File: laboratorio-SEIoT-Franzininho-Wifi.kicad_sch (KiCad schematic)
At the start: 139 parts, among them J1 Conn_01x20, J2 Conn_01x20, J3 Grove, J4 Grove, M1 Motor_Servo, Q1 BC547, SW1 SW_Push_Dual, SW10 SW_Push_Dual, SW11 SW_Push_Dual, SW12 SW_Push_Dual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

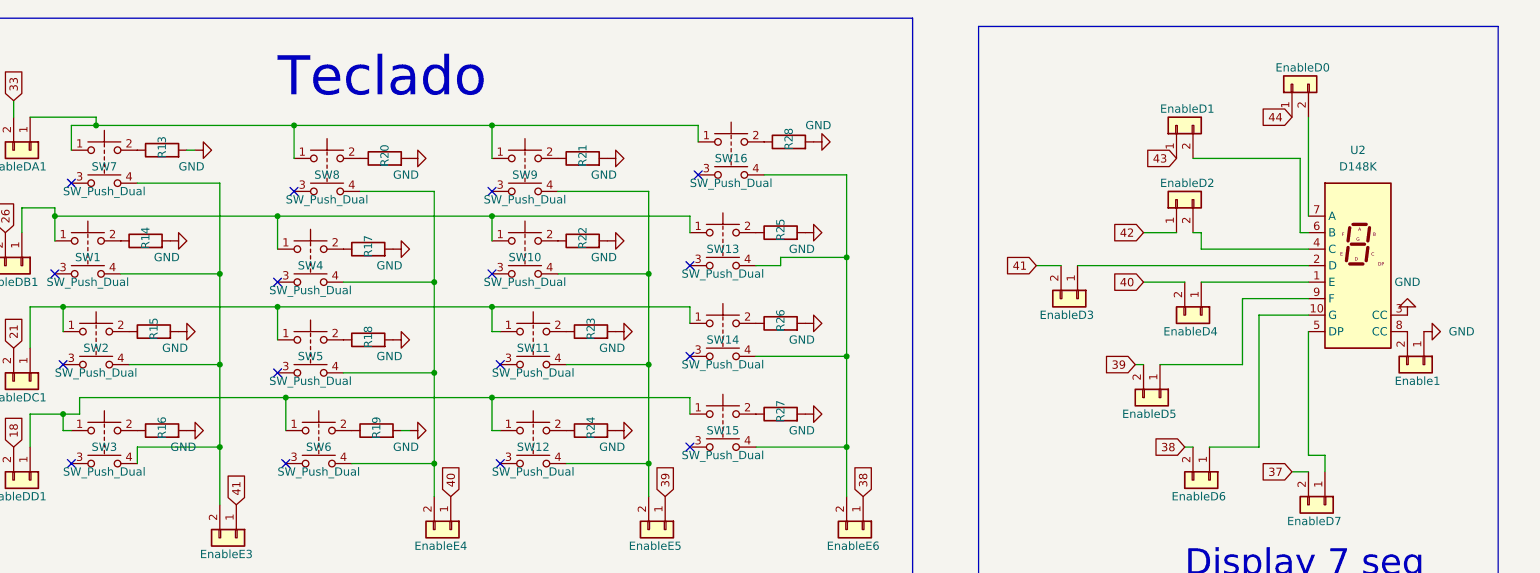
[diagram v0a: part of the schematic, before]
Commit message: correção de conexão no display de 7 segmentos
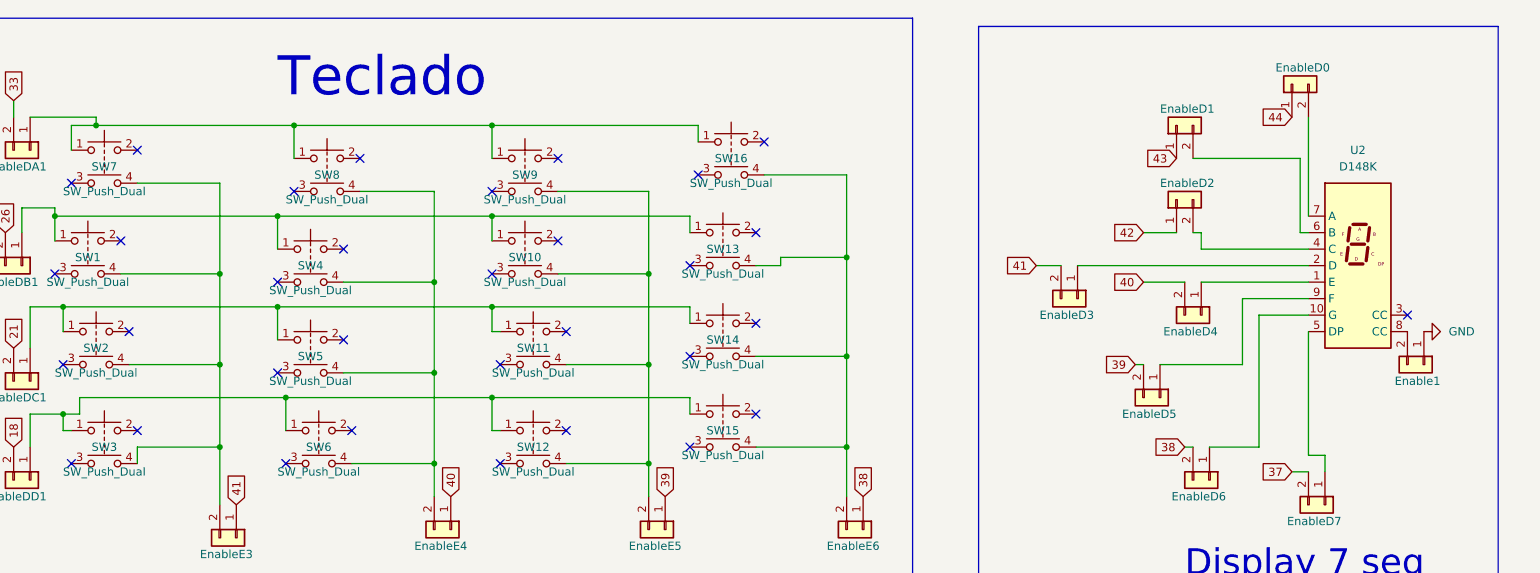
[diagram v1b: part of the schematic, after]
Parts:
- removed R13, R14, R15, R16, R17, R18, R19, R20, R21, R22, R23, R24, R25, R26, R27, R28: R, Resistor_SMD:R_0805_2012Metric, symbol Device:R
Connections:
- net GND: no longer U2.3 (CC)
- no-connect marks 24 -> 41
